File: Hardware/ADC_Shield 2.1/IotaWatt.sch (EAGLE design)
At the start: 58 parts, among them J0 STEREO_JACK_BOT, J1 STEREO_JACK_BOT, J2 STEREO_JACK_BOT, J3 STEREO_JACK_BOT, J4 STEREO_JACK_BOT, J5 STEREO_JACK_BOT, J6 STEREO_JACK_BOT

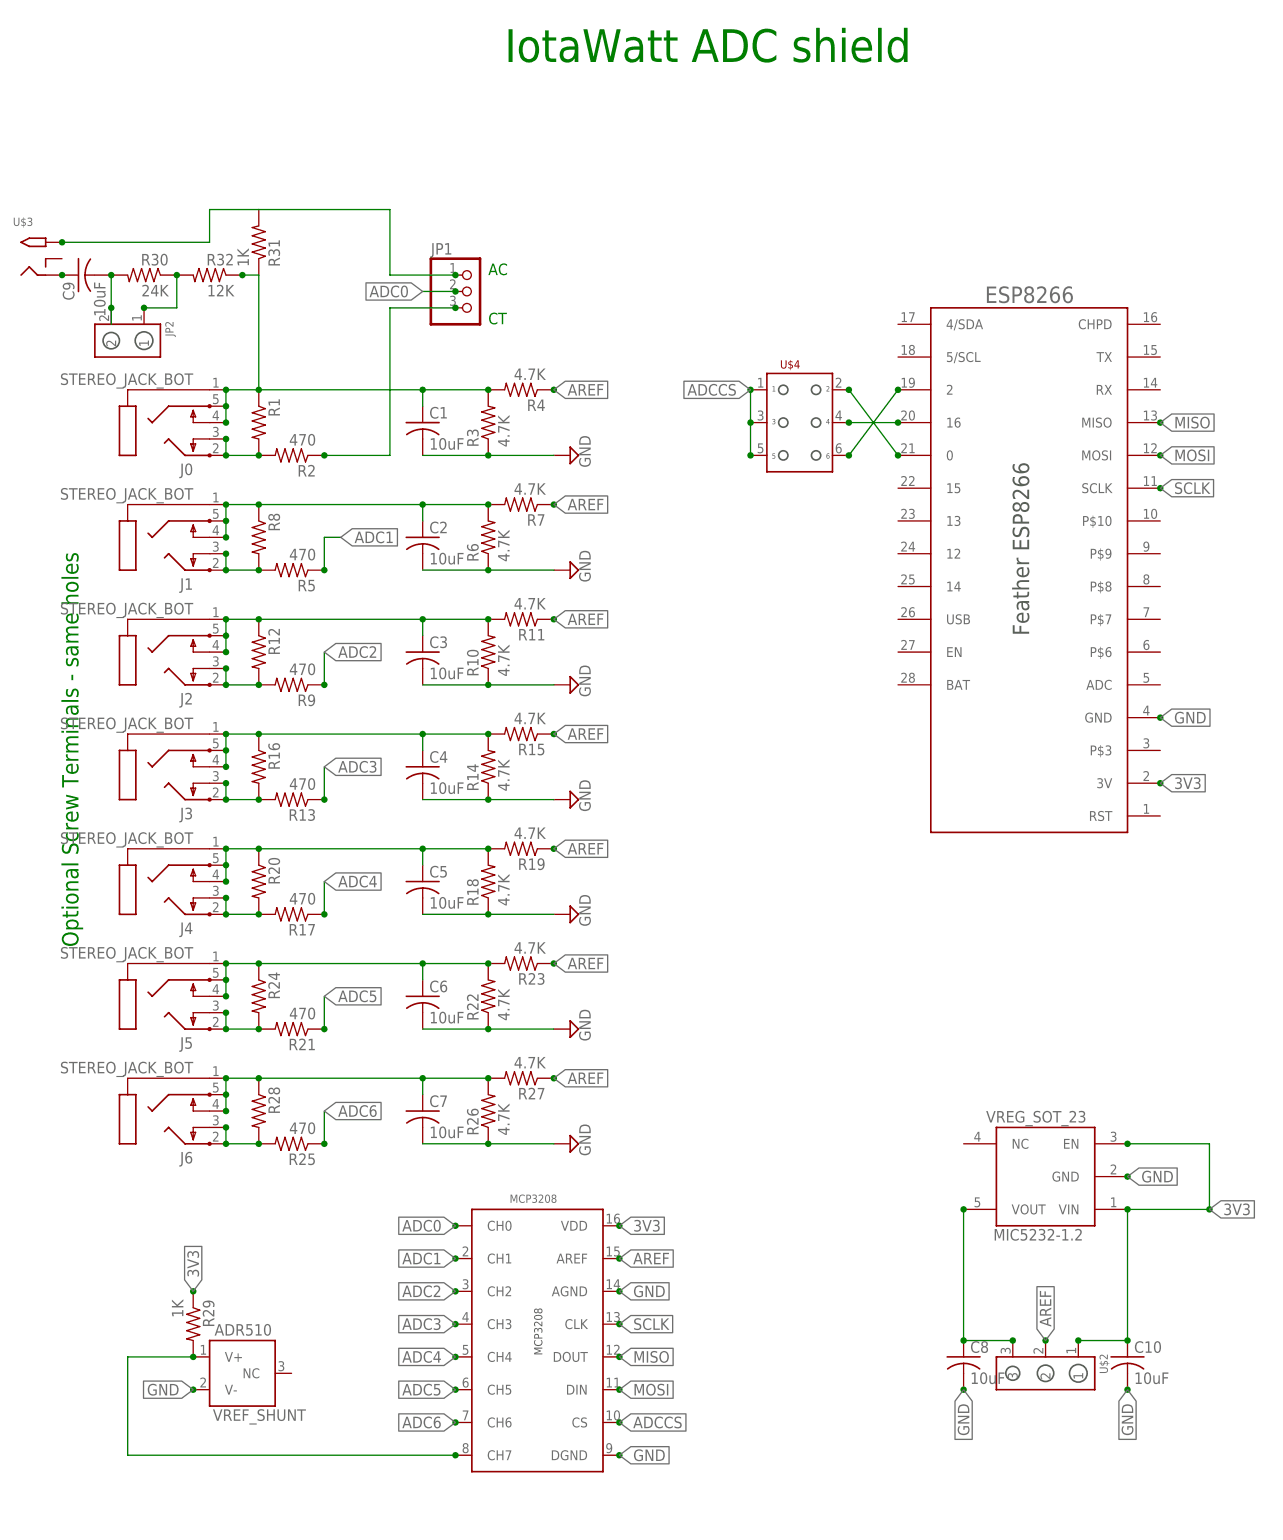
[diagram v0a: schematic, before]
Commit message: Add index to logfile and other significant changes.
Adds an index file to the SD that identifies gaps in the regular
intervals of entries.  A second level index is created in memory to
further increase API performance.  Added VT phase calibration aids.
Other improvements to config/status app.
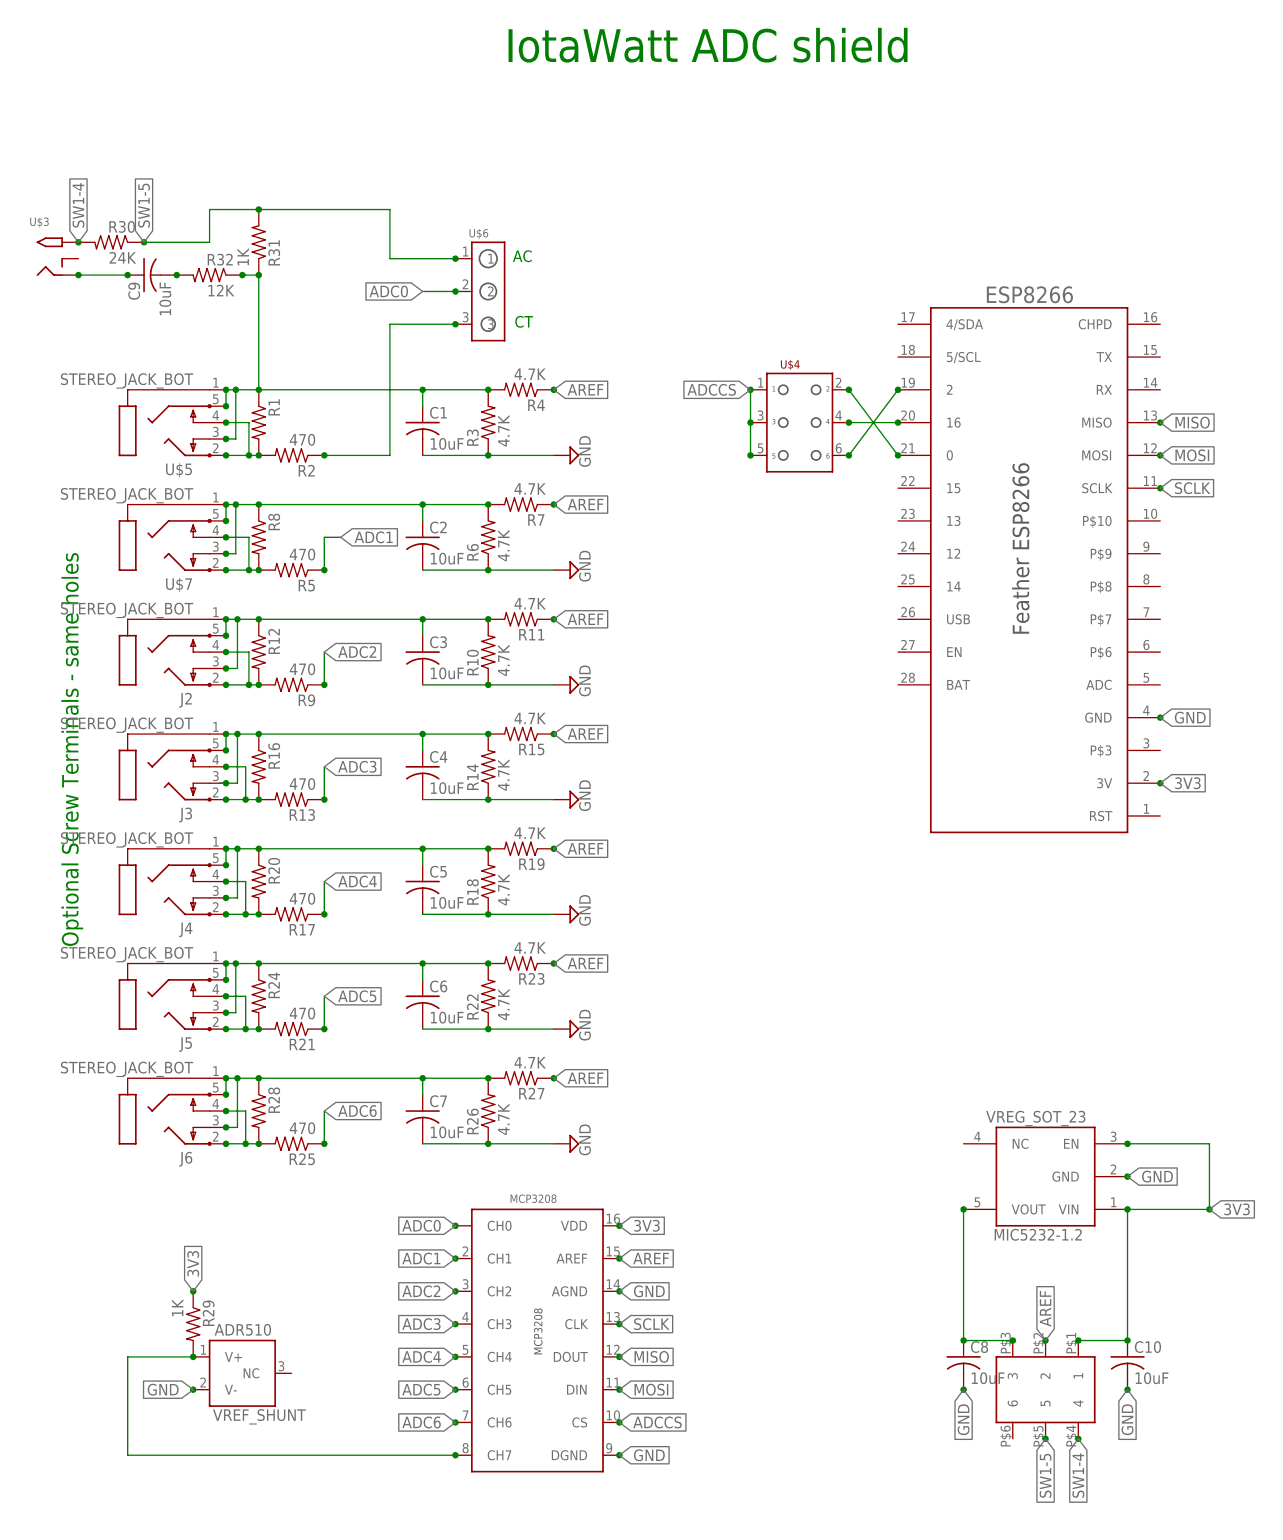
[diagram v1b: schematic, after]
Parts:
- removed JP1: (no value), adafruit:PINHD-1X3
- removed JP2: HEADER_1X2, IotaWatt_parts:HEADER_1X2
- removed U$2: HEADER_1X3, IotaWatt_parts:HEADER_1X3
- added U$6: HEADER_1X3, IotaWatt_parts:HEADER_1X3
- added U$8: DPDT_SMT_SW, IotaWatt_parts:DPDT_SMT_SW
- renumbered J0 to U$5, J1 to U$7
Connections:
- removed net ACV1: C9.2, JP2.2, R30.2
- removed net ACV2: JP2.1, R30.1, R32.2
- removed net N$8: JP1.1, R31.2, U$3.TIP
- new net N$11: R1.2, R2.2, U$5.3, U$5.5
- new net SW1-4: R30.2, U$3.TIP, U$8.4
- new net SW1-5: R30.1, R31.2, U$6.1, U$8.5
- net 3V3: now also U$8.1; no longer U$2.1
- net ADC0: now also U$6.2; no longer JP1.2
- net AREF: now also U$8.2; no longer U$2.2
- net N$1: now also U$6.3; no longer JP1.3
- net N$12: now also J2.4; no longer J2.3
- net N$13: now also J4.4; no longer J4.3
- net N$14: now also J5.3; no longer J5.4
- net N$16: now also J5.4; no longer J5.3
- net N$17: now also C9.2, R32.2; no longer R1.2, R2.2, U$5.4, U$5.5
- net N$18: now also J6.3; no longer J6.4
- net N$19: now also J6.4; no longer J6.3
- net N$2: now also U$5.4; no longer U$5.3
- net N$20: now also U$7.3; no longer U$7.4
- net N$21: now also J3.3; no longer J3.4
- net N$22: now also J3.4; no longer J3.3
- net N$24: now also U$8.3; no longer U$2.3
- net N$26: now also J4.3; no longer J4.4
- net N$4: now also U$7.4; no longer U$7.3
- net N$5: now also J2.3; no longer J2.4
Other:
- moved on the sheet: C9, R30, U$3
